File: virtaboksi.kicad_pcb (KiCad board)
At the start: 2 copper layers, 50 x 72 mm, 66 parts, among them J1 Panel_01x06, J2 External_01x06, J3 Optional_01x03, J5 Powerpole 01x02, J6 Powerpole 01x02, J7 Powerpole 01x02, J8 TagConnect_TC2030-NL, Q1 2N7002, Q10 MMBT3906, Q11 MMBT3906, Q12 MMBT3906, Q13 MMBT3906, Q2 IRF4905, Q3 IRF4905, Q4 2N7002, Q5 IRF4905, Q6 IRF4905, Q7 2N7002, Q8 IRF4905, Q9 IRF4905, U1 SRV05-4, U2 AMSRI-783.3-NZ, U3 SRV05-4, U4 SP3485EN, U5 STM8S003F3P

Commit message: Incorrect part number spotted before production, 1.5kohm -> 4.7kohm
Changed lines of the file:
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@@
     (fp_line (start -2.95 -3.5) (end -2.95 -4.75) (layer "F.Fab") (width 0.1))
     (fp_line (start -2.45 -4.25) (end -2.45 3) (layer "F.Fab") (width 0.1))
-    (pad "1" thru_hole roundrect (at 0 0) (size 1.8 3.6) (drill 1.2) (layers *.Cu *.Mask) (roundrect_rratio 0.138889)
+    (pad "1" thru_hole roundrect (at 0 0) (size 1.8 3.6) (drill 1.2) (layers *.Cu *.Mask) (roundrect_rratio 0.1388888889)
       (net 6 "+3.3V") (pinfunction "Pin_1") (pintype "passive"))
     (pad "2" thru_hole oval (at 3.5 0) (size 1.8 3.6) (drill 1.2) (layers *.Cu *.Mask)
@@
     (fp_line (start 19.95 3) (end 19.95 -4.25) (layer "F.Fab") (width 0.1))
     (fp_line (start -2.95 -3.5) (end -2.95 -4.75) (layer "F.Fab") (width 0.1))
-    (pad "1" thru_hole roundrect (at 0 0) (size 1.8 3.6) (drill 1.2) (layers *.Cu *.Mask) (roundrect_rratio 0.138889)
+    (pad "1" thru_hole roundrect (at 0 0) (size 1.8 3.6) (drill 1.2) (layers *.Cu *.Mask) (roundrect_rratio 0.1388888889)
       (net 43 "/IN1") (pinfunction "Pin_1") (pintype "passive"))
     (pad "2" thru_hole oval (at 3.5 0) (size 1.8 3.6) (drill 1.2) (layers *.Cu *.Mask)
@@
     (descr "Resistor SMD 0603 (1608 Metric), square (rectangular) end terminal, IPC_7351 nominal, (Body size source: IPC-SM-782 page 72, https://www.pcb-3d.com/wordpress/wp-content/uploads/ipc-sm-782a_amendment_1_and_2.pdf), generated with kicad-footprint-generator")
     (tags "resistor")
-    (property "LCSC" "C22843")
+    (property "LCSC" "C23162")
     (property "Sheetfile" "virtaboksi.kicad_sch")
     (property "Sheetname" "")
@@
     (fp_line (start 1.6 -0.8) (end 1.6 0.8) (layer "F.Fab") (width 0.1))
     (fp_line (start -1.6 -0.8) (end 1.6 -0.8) (layer "F.Fab") (width 0.1))
-    (pad "1" smd roundrect (at -1.475 0) (size 1.15 1.8) (layers "F.Cu" "F.Paste" "F.Mask") (roundrect_rratio 0.217391)
+    (pad "1" smd roundrect (at -1.475 0) (size 1.15 1.8) (layers "F.Cu" "F.Paste" "F.Mask") (roundrect_rratio 0.2173913043)
       (net 5 "Net-(C1-Pad1)") (pintype "passive"))
-    (pad "2" smd roundrect (at 1.475 0) (size 1.15 1.8) (layers "F.Cu" "F.Paste" "F.Mask") (roundrect_rratio 0.217391)
+    (pad "2" smd roundrect (at 1.475 0) (size 1.15 1.8) (layers "F.Cu" "F.Paste" "F.Mask") (roundrect_rratio 0.2173913043)
       (net 1 "GND") (pintype "passive"))
     (model "${KICAD6_3DMODEL_DIR}/Capacitor_SMD.3dshapes/C_1206_3216Metric.wrl"
@@
     (descr "Resistor SMD 0603 (1608 Metric), square (rectangular) end terminal, IPC_7351 nominal, (Body size source: IPC-SM-782 page 72, https://www.pcb-3d.com/wordpress/wp-content/uploads/ipc-sm-782a_amendment_1_and_2.pdf), generated with kicad-footprint-generator")
     (tags "resistor")
-    (property "LCSC" "C22843")
+    (property "LCSC" "C23162")
     (property "Sheetfile" "virtaboksi.kicad_sch")
     (property "Sheetname" "")
@@
     (descr "Resistor SMD 0603 (1608 Metric), square (rectangular) end terminal, IPC_7351 nominal, (Body size source: IPC-SM-782 page 72, https://www.pcb-3d.com/wordpress/wp-content/uploads/ipc-sm-782a_amendment_1_and_2.pdf), generated with kicad-footprint-generator")
     (tags "resistor")
-    (property "LCSC" "C22843")
+    (property "LCSC" "C23162")
     (property "Sheetfile" "virtaboksi.kicad_sch")
     (property "Sheetname" "")
@@
     (descr "Resistor SMD 0603 (1608 Metric), square (rectangular) end terminal, IPC_7351 nominal, (Body size source: IPC-SM-782 page 72, https://www.pcb-3d.com/wordpress/wp-content/uploads/ipc-sm-782a_amendment_1_and_2.pdf), generated with kicad-footprint-generator")
     (tags "resistor")
-    (property "LCSC" "C22843")
+    (property "LCSC" "C23162")
     (property "Sheetfile" "virtaboksi.kicad_sch")
     (property "Sheetname" "")
@@
   (gr_line (start 156 37) (end 155.985786 104.985786) (layer "Edge.Cuts") (width 0.1))
   (gr_line (start 108.014214 35.014214) (end 154 35) (layer "Edge.Cuts") (width 0.1))
-  (gr_text "⏚" (at 129.4 41.3) (layer "B.SilkS")
+  (gr_text "⏚" (at 129.9 41.4) (layer "B.SilkS")
     (effects (font (size 1.5 1.5) (thickness 0.3)) (justify mirror))
   )
-  (gr_text "TX" (at 131.9 40.1 90) (layer "B.SilkS")
+  (gr_text "TX" (at 132.4 40.2 90) (layer "B.SilkS")
     (effects (font (size 1.5 1.5) (thickness 0.3)) (justify left mirror))
   )
-  (gr_text "RX" (at 134.4 40 90) (layer "B.SilkS")
+  (gr_text "RX" (at 134.9 40.1 90) (layer "B.SilkS")
     (effects (font (size 1.5 1.5) (thickness 0.3)) (justify left mirror))
   )

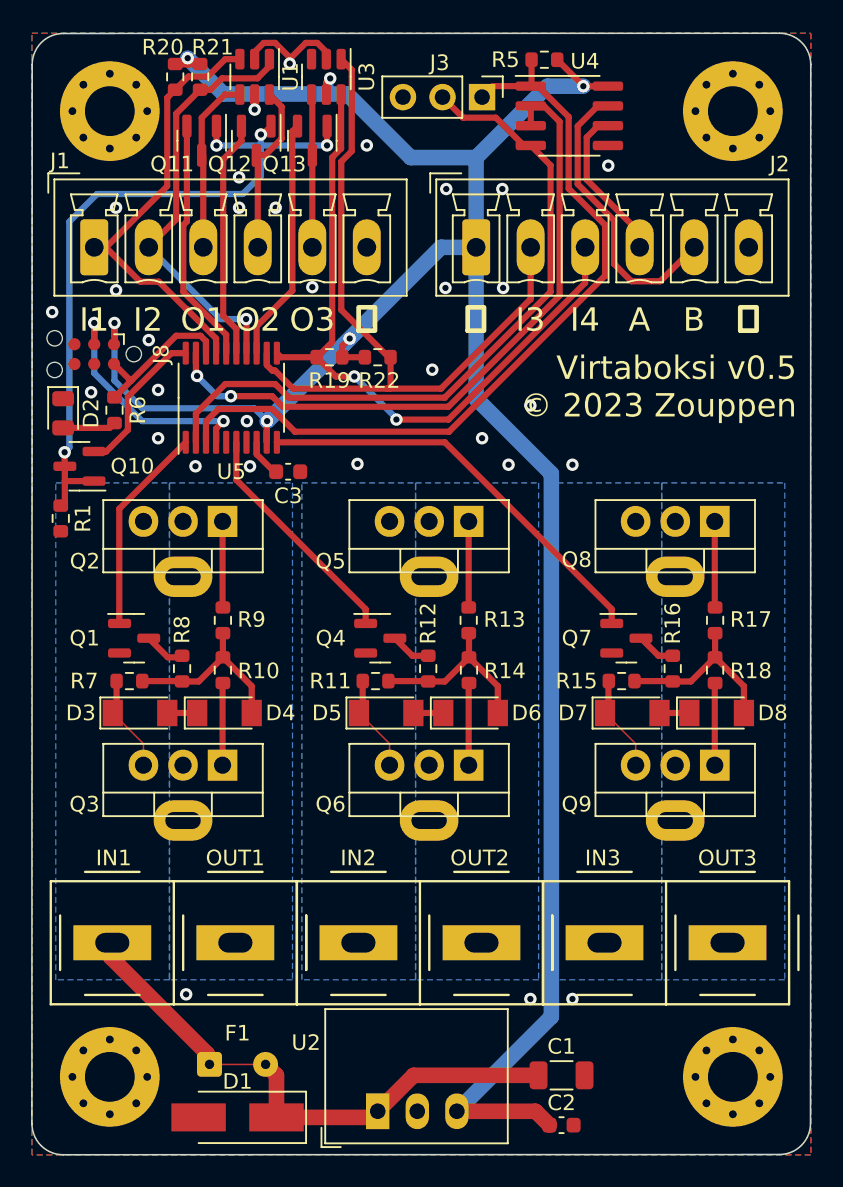
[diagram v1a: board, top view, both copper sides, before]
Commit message: Make clearance larger for power lines and relief smaller for ground (both now 0.4mm)
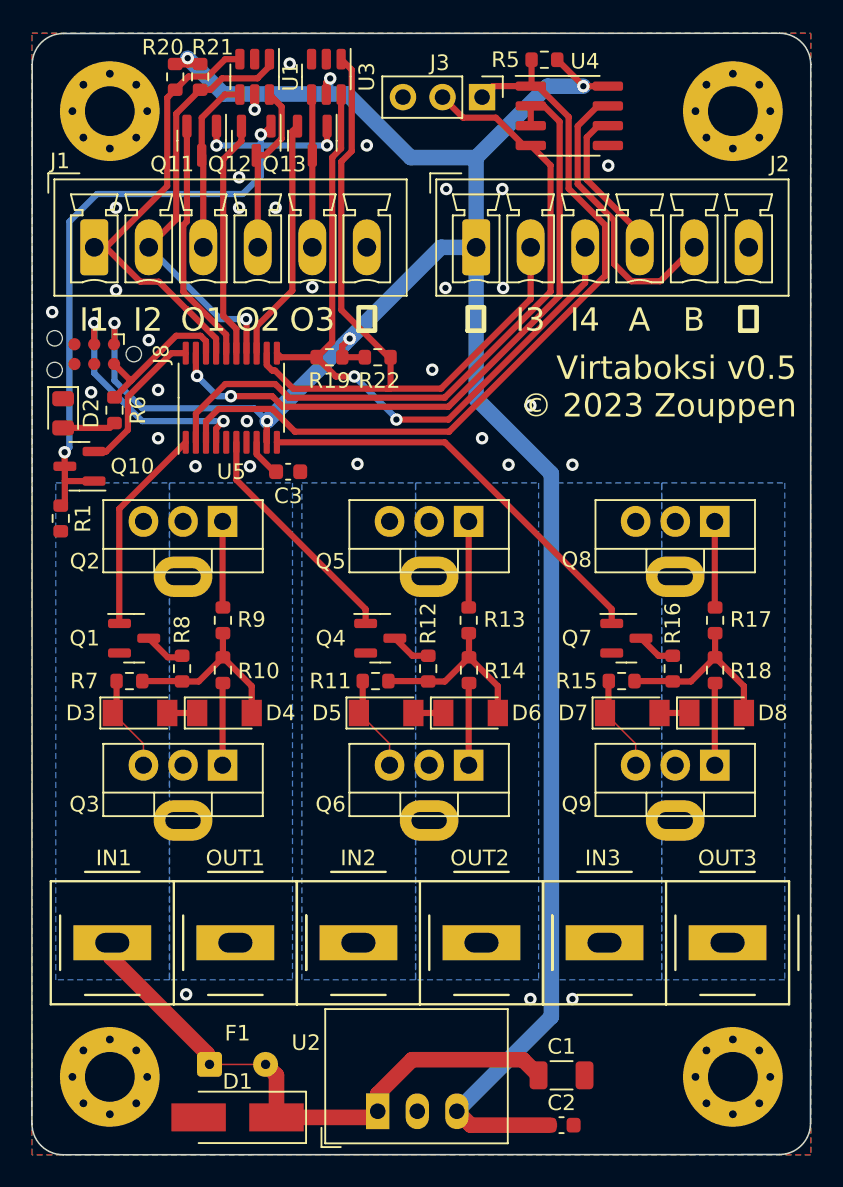
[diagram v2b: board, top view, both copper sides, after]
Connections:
- net Net-(C1-Pad1) renamed /PWR1
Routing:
- net GND: track 7.94 -> 0.42 mm
- net /PWR1: track 21.6 -> 23.1 mm
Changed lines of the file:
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@@
   (net 3 "/GROUP2 IN")
   (net 4 "/GROUP3 IN")
-  (net 5 "Net-(C1-Pad1)")
+  (net 5 "/PWR1")
   (net 6 "+3.3V")
   (net 7 "/GROUP2 CTRL")
@@
     (fp_line (start -3.31 1) (end -3.31 -6.5) (layer "F.Fab") (width 0.1))
     (pad "1" thru_hole rect (at 0 0) (size 1.5 2.3) (drill 1) (layers *.Cu *.Mask)
-      (net 5 "Net-(C1-Pad1)") (pinfunction "IN") (pintype "power_in"))
+      (net 5 "/PWR1") (pinfunction "IN") (pintype "power_in"))
     (pad "2" thru_hole oval (at 2.54 0) (size 1.5 2.3) (drill 1) (layers *.Cu *.Mask)
       (net 1 "GND") (pinfunction "GND") (pintype "power_in"))
@@
     (fp_line (start -1.6 -0.8) (end 1.6 -0.8) (layer "F.Fab") (width 0.1))
     (pad "1" smd roundrect (at -1.475 0) (size 1.15 1.8) (layers "F.Cu" "F.Paste" "F.Mask") (roundrect_rratio 0.2173913043)
-      (net 5 "Net-(C1-Pad1)") (pintype "passive"))
+      (net 5 "/PWR1") (pintype "passive"))
     (pad "2" smd roundrect (at 1.475 0) (size 1.15 1.8) (layers "F.Cu" "F.Paste" "F.Mask") (roundrect_rratio 0.2173913043)
       (net 1 "GND") (pintype "passive"))
@@
       (net 2 "/GROUP1 IN") (pintype "passive"))
     (pad "2" thru_hole circle (at 3.6 0) (size 1.6 1.6) (drill 0.6) (layers *.Cu *.Mask)
-      (net 5 "Net-(C1-Pad1)") (pintype "passive"))
+      (net 5 "/PWR1") (pintype "passive"))
     (zone (net 0) (net_name "") (layer "F.Cu") (hatch edge 0.508)
       (connect_pads (clearance 0))
@@
     (fp_line (start 0.50118 0.75032) (end 0.50118 -0.79908) (layer "F.Fab") (width 0.1))
     (pad "1" smd rect (at -2.5 0 180) (size 3.5 1.8) (layers "F.Cu" "F.Paste" "F.Mask")
-      (net 5 "Net-(C1-Pad1)") (pinfunction "A1") (pintype "passive"))
+      (net 5 "/PWR1") (pinfunction "A1") (pintype "passive"))
     (pad "2" smd rect (at 2.5 0 180) (size 3.5 1.8) (layers "F.Cu" "F.Paste" "F.Mask")
       (net 1 "GND") (pinfunction "A2") (pintype "passive"))
@@
     (style (thickness 0.15) (arrow_length 1.27) (text_position_mode 0) (extension_height 0.58642) (extension_offset 0.5) keep_text_aligned)
   )
-  (segment (start 124.9 36.2) (end 124.32 35.62) (width 0.4) (layer "F.Cu") (net 1))
-  (segment (start 120.3 36.6625) (end 120.3 36.2) (width 0.4) (layer "F.Cu") (net 1))
-  (segment (start 122.55 36.550467) (end 122.55 36.95) (width 0.4) (layer "F.Cu") (net 1))
-  (segment (start 120.88 35.62) (end 121.619533 35.62) (width 0.4) (layer "F.Cu") (net 1))
   (segment (start 124.9 36.7) (end 124.9 37.124533) (width 0.4) (layer "F.Cu") (net 1))
-  (segment (start 122.55 36.650467) (end 122.55 36.95) (width 0.4) (layer "F.Cu") (net 1))
-  (segment (start 124.32 35.62) (end 123.580467 35.62) (width 0.4) (layer "F.Cu") (net 1))
-  (segment (start 121.619533 35.62) (end 122.55 36.550467) (width 0.4) (layer "F.Cu") (net 1))
-  (segment (start 123.580467 35.62) (end 122.55 36.650467) (width 0.4) (layer "F.Cu") (net 1))
-  (segment (start 124.9 36.6625) (end 124.9 36.2) (width 0.4) (layer "F.Cu") (net 1))
-  (segment (start 120.3 36.2) (end 120.88 35.62) (width 0.4) (layer "F.Cu") (net 1))
   (via (at 119.8 59.9) (size 0.8) (drill 0.4) (layers "F.Cu" "B.Cu") (free) (net 1))
   (via (at 116.5 62.8) (size 0.8) (drill 0.4) (layers "F.Cu" "B.Cu") (free) (net 1))
@@
   (segment (start 143.01 76.765) (end 143.035 76.74) (width 0.4) (layer "F.Cu") (net 4))
   (segment (start 143.01 78.64) (end 143.01 76.765) (width 0.4) (layer "F.Cu") (net 4))
+  (segment (start 137.525 100.9) (end 130.4 100.9) (width 1) (layer "F.Cu") (net 5))
+  (segment (start 138.525 101.9) (end 137.525 100.9) (width 1) (layer "F.Cu") (net 5))
+  (segment (start 128.2 103.1) (end 128.2 104.2075) (width 1) (layer "F.Cu") (net 5))
   (segment (start 121.7 104.6) (end 121.7 101.9) (width 1) (layer "F.Cu") (net 5))
-  (segment (start 138.525 101.9) (end 130.5075 101.9) (width 1) (layer "F.Cu") (net 5))
   (segment (start 127.8075 104.6) (end 128.2 104.2075) (width 1) (layer "F.Cu") (net 5))
-  (segment (start 130.5075 101.9) (end 128.2 104.2075) (width 1) (layer "F.Cu") (net 5))
+  (segment (start 130.4 100.9) (end 128.2 103.1) (width 1) (layer "F.Cu") (net 5))
   (segment (start 121.7 101.9) (end 121 101.2) (width 1) (layer "F.Cu") (net 5))
   (segment (start 121.7 104.6) (end 127.8075 104.6) (width 1) (layer "F.Cu") (net 5))
   (segment (start 124.9 38.15) (end 125.15 37.9) (width 0.4) (layer "F.Cu") (net 6))
+  (segment (start 139.225 105.1) (end 134.1725 105.1) (width 1) (layer "F.Cu") (net 6))
   (segment (start 141.4 38.4) (end 142.97 38.4) (width 0.4) (layer "F.Cu") (net 6))
   (segment (start 124.9 38.9375) (end 124.9 38.15) (width 0.4) (layer "F.Cu") (net 6))
   (segment (start 115.225 37) (end 115.2 36.975) (width 0.4) (layer "F.Cu") (net 6))
+  (segment (start 134.1725 105.1) (end 133.28 104.2075) (width 1) (layer "F.Cu") (net 6))
   (segment (start 111.3 53.6) (end 111.3 54.935) (width 0.4) (layer "F.Cu") (net 6))
   (segment (start 127.375 55.8) (end 125.925 55.8) (width 0.4) (layer "F.Cu") (net 6))
-  (segment (start 138.3325 104.2075) (end 139.225 105.1) (width 1) (layer "F.Cu") (net 6))
   (segment (start 141.4 38.4) (end 141.4 38.375) (width 0.4) (layer "F.Cu") (net 6))
   (segment (start 116 36.6) (end 116 37) (width 0.4) (layer "F.Cu") (net 6))
@@
   (segment (start 120.3 39.9) (end 120.3 38.9375) (width 0.4) (layer "F.Cu") (net 6))
   (segment (start 125.925 55.075) (end 126.4 54.6) (width 0.4) (layer "F.Cu") (net 6))
-  (segment (start 133.28 104.2075) (end 138.3325 104.2075) (width 1) (layer "F.Cu") (net 6))
   (segment (start 121.075 61.2625) (end 121.075 60.496177) (width 0.4) (layer "F.Cu") (net 6))
   (segment (start 116.8 37) (end 116 37) (width 0.4) (layer "F.Cu") (net 6))
@@
     (connect_pads (clearance 0.2))
     (min_thickness 0.254) (filled_areas_thickness no)
-    (fill yes (thermal_gap 0.508) (thermal_bridge_width 1))
+    (fill yes (thermal_gap 0.4) (thermal_bridge_width 1))
     (polygon
       (pts

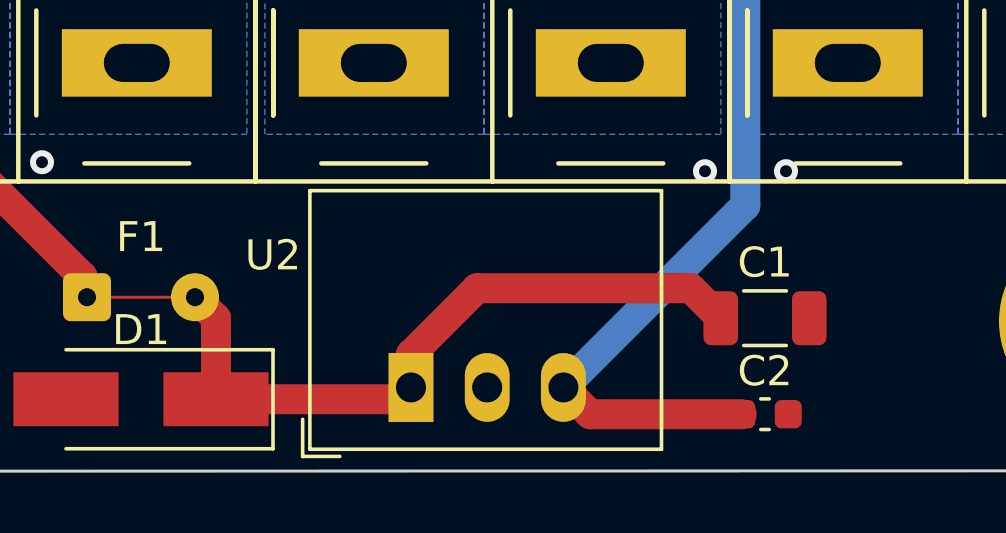
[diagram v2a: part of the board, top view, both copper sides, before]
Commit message: Move capacitors so that traces make up direct lines
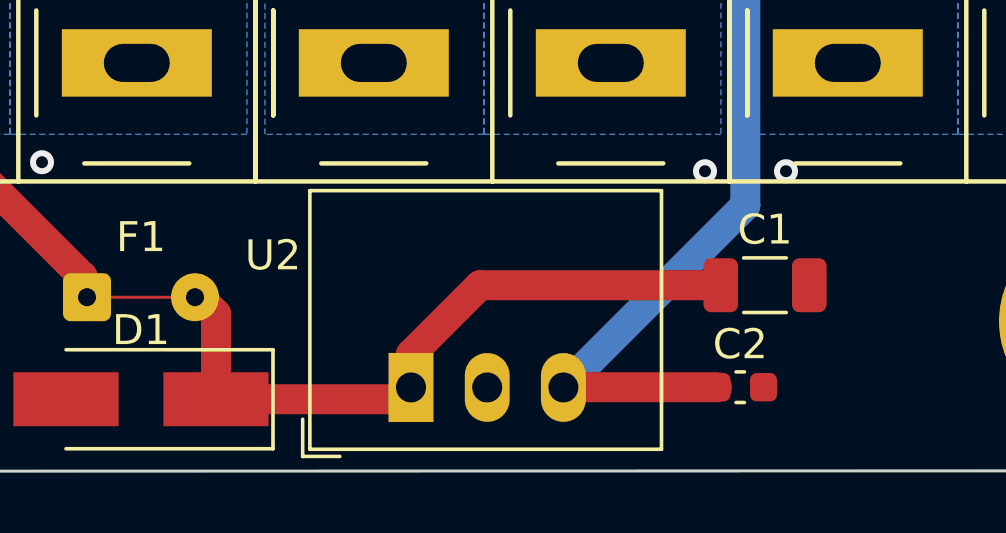
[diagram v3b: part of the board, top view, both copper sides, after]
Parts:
- moved C2 1.22 mm to (139.2, 104.2)
- moved C1 1.10 mm to (140.0, 100.8)
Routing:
- net +3.3V: track 150.8 -> 149.6 mm
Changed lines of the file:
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@@
   )
   (footprint "Capacitor_SMD:C_1206_3216Metric" (layer "F.Cu")
-    (at 140 101.9)
+    (at 140 100.8)
     (descr "Capacitor SMD 1206 (3216 Metric), square (rectangular) end terminal, IPC_7351 nominal, (Body size source: IPC-SM-782 page 76, https://www.pcb-3d.com/wordpress/wp-content/uploads/ipc-sm-782a_amendment_1_and_2.pdf), generated with kicad-footprint-generator")
     (tags "capacitor")
@@
   )
   (footprint "Capacitor_SMD:C_0603_1608Metric" (layer "F.Cu")
-    (at 140 105.1)
+    (at 139.175 104.2)
     (descr "Capacitor SMD 0603 (1608 Metric), square (rectangular) end terminal, IPC_7351 nominal, (Body size source: IPC-SM-782 page 76, https://www.pcb-3d.com/wordpress/wp-content/uploads/ipc-sm-782a_amendment_1_and_2.pdf), generated with kicad-footprint-generator")
     (tags "capacitor")
@@
   (segment (start 143.01 76.765) (end 143.035 76.74) (width 0.4) (layer "F.Cu") (net 4))
   (segment (start 143.01 78.64) (end 143.01 76.765) (width 0.4) (layer "F.Cu") (net 4))
-  (segment (start 137.525 100.9) (end 130.4 100.9) (width 1) (layer "F.Cu") (net 5))
-  (segment (start 138.525 101.9) (end 137.525 100.9) (width 1) (layer "F.Cu") (net 5))
-  (segment (start 128.2 103.1) (end 128.2 104.2075) (width 1) (layer "F.Cu") (net 5))
-  (segment (start 121.7 104.6) (end 121.7 101.9) (width 1) (layer "F.Cu") (net 5))
+  (segment (start 130.5 100.8) (end 138.525 100.8) (width 1) (layer "F.Cu") (net 5))
+  (segment (start 121.7 104.6) (end 121.7 101.75) (width 1) (layer "F.Cu") (net 5))
+  (segment (start 128.2 104.2075) (end 128.2 103.1) (width 1) (layer "F.Cu") (net 5))
   (segment (start 127.8075 104.6) (end 128.2 104.2075) (width 1) (layer "F.Cu") (net 5))
-  (segment (start 130.4 100.9) (end 128.2 103.1) (width 1) (layer "F.Cu") (net 5))
-  (segment (start 121.7 101.9) (end 121 101.2) (width 1) (layer "F.Cu") (net 5))
+  (segment (start 121.7 101.75) (end 121.15 101.2) (width 1) (layer "F.Cu") (net 5))
   (segment (start 121.7 104.6) (end 127.8075 104.6) (width 1) (layer "F.Cu") (net 5))
+  (segment (start 128.2 103.1) (end 130.5 100.8) (width 1) (layer "F.Cu") (net 5))
   (segment (start 124.9 38.15) (end 125.15 37.9) (width 0.4) (layer "F.Cu") (net 6))
-  (segment (start 139.225 105.1) (end 134.1725 105.1) (width 1) (layer "F.Cu") (net 6))
   (segment (start 141.4 38.4) (end 142.97 38.4) (width 0.4) (layer "F.Cu") (net 6))
   (segment (start 124.9 38.9375) (end 124.9 38.15) (width 0.4) (layer "F.Cu") (net 6))
   (segment (start 115.225 37) (end 115.2 36.975) (width 0.4) (layer "F.Cu") (net 6))
-  (segment (start 134.1725 105.1) (end 133.28 104.2075) (width 1) (layer "F.Cu") (net 6))
   (segment (start 111.3 53.6) (end 111.3 54.935) (width 0.4) (layer "F.Cu") (net 6))
+  (segment (start 138.4 104.2) (end 133.2875 104.2) (width 1) (layer "F.Cu") (net 6))
   (segment (start 127.375 55.8) (end 125.925 55.8) (width 0.4) (layer "F.Cu") (net 6))
   (segment (start 141.4 38.4) (end 141.4 38.375) (width 0.4) (layer "F.Cu") (net 6))
   (segment (start 116 36.6) (end 116 37) (width 0.4) (layer "F.Cu") (net 6))
   (segment (start 111.3 54.935) (end 111.27 54.965) (width 0.4) (layer "F.Cu") (net 6))
+  (segment (start 133.2875 104.2) (end 133.28 104.2075) (width 1) (layer "F.Cu") (net 6))
   (segment (start 116 37) (end 115.225 37) (width 0.4) (layer "F.Cu") (net 6))
   (segment (start 121.075 59.925) (end 121.1 59.9) (width 0.4) (layer "F.Cu") (net 6))

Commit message: Change bidirectional TVS to unidirectional
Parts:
- D1: value P6SMAJ33CA -> SMAJ33A
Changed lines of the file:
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@@
     (descr "Diode SMA (DO-214AC) Handsoldering")
     (tags "Diode SMA (DO-214AC) Handsoldering")
-    (property "LCSC" "C3019524")
+    (property "LCSC" "C353454")
     (property "Sheetfile" "virtaboksi.kicad_sch")
     (property "Sheetname" "")
@@
       (effects (font (size 1 1) (thickness 0.15)))
     )
-    (fp_text value "P6SMAJ33CA" (at 0 2.6) (layer "F.Fab")
+    (fp_text value "SMAJ33A" (at 0 2.6) (layer "F.Fab")
       (effects (font (size 1 1) (thickness 0.15)))
     )
